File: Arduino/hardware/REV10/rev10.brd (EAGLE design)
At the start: 68.6 x 53.3 mm, 43 parts, among them IC2 ATMEGA168-AU, Q1 32768Hz, Q2 BSS84, U1 TC1185SMD, U2 ARDUINOR3-DIMENSION

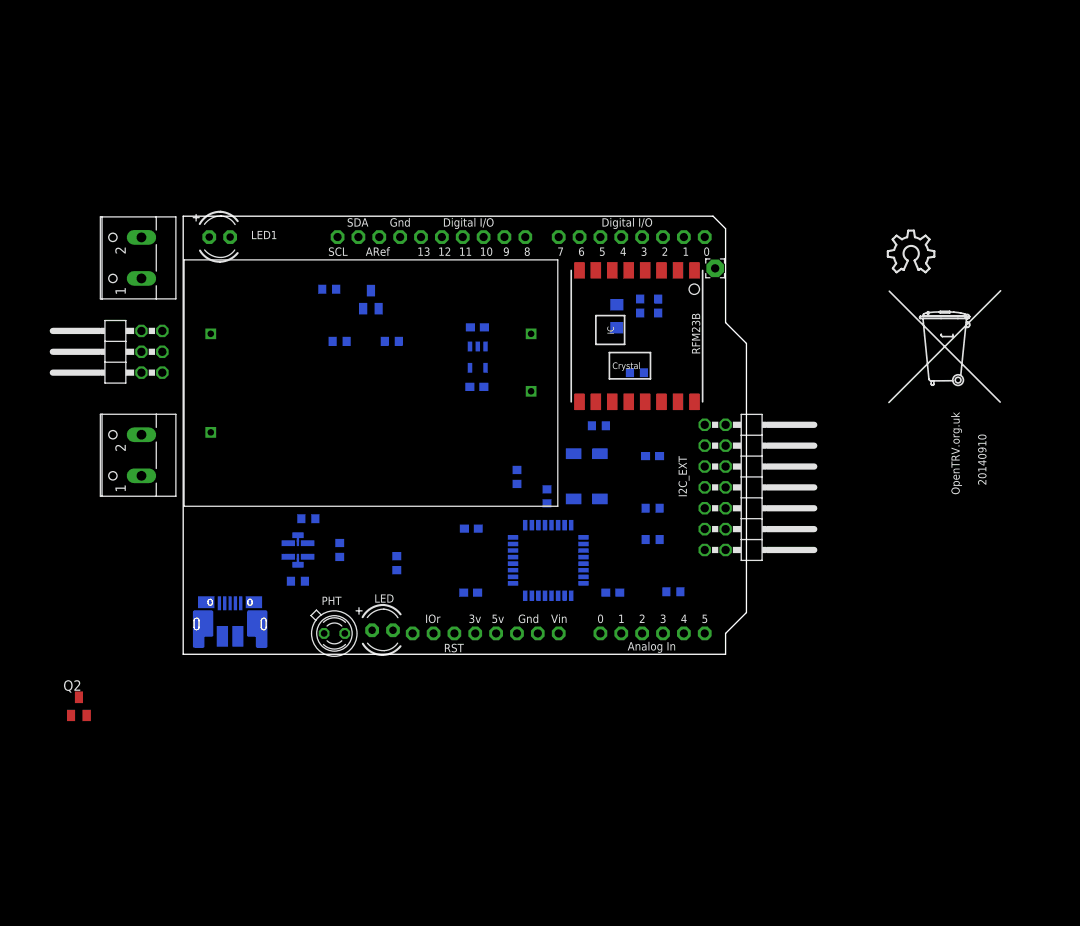
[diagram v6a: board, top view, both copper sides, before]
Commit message: added relay on board
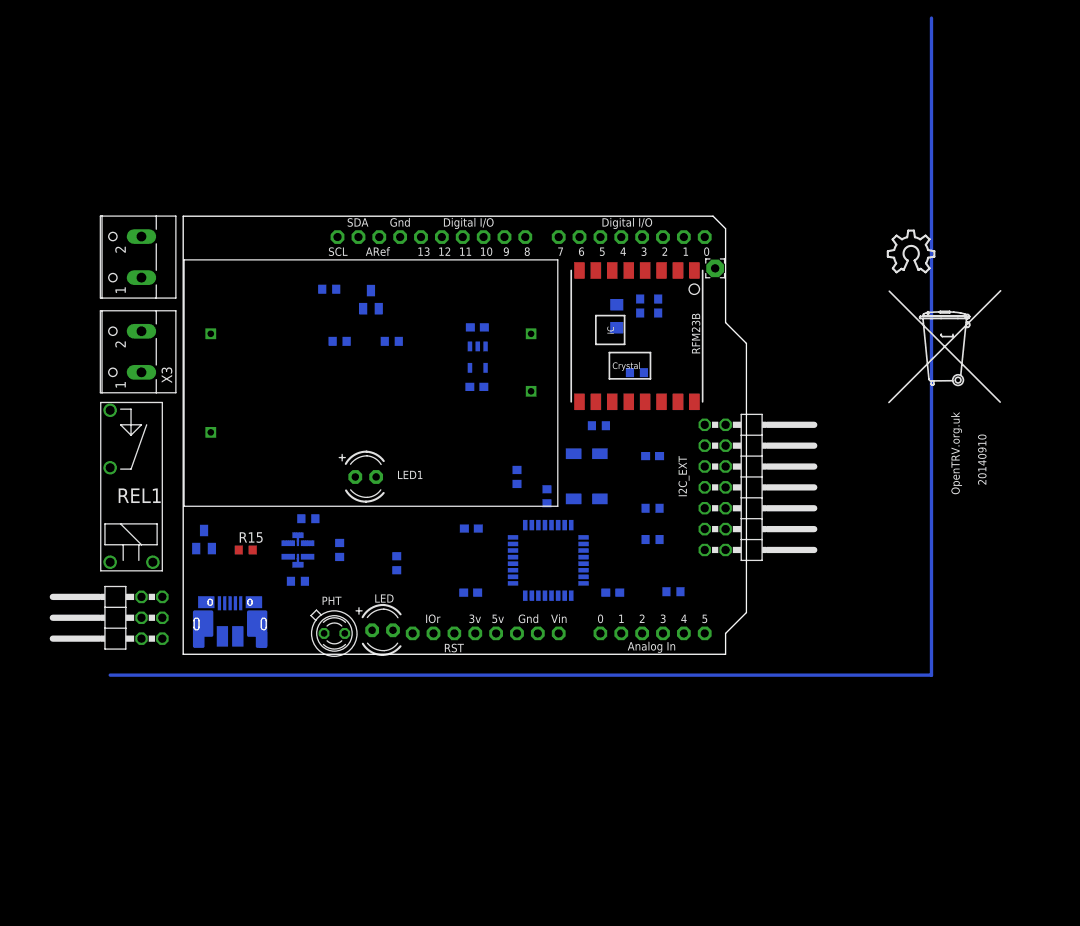
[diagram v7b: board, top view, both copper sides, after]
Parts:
- removed X2: (no value), con-wago-500:W237-102
- added R15: 4.7K, resistor:R0603
- added REL1: (no value), ALDP105:ALDP105
- added X3: (no value), con-wago-500:W237-102
- moved LED1 34.2 mm to (31.1, 21.6)
- moved JP2 32.4 mm to (0.00, 4.45)
- moved Q2 25.4 mm to (11.4, 14.0), flipped to the bottom
- moved X1 24.1 mm to (2.54, 48.4)
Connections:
- new net 5VGSM: Q2.3
- new net N$17: Q2.1, R15.1
- new net N$22: REL1.C, X3.2
- new net N$24: REL1.S, X3.1
- new net PFET: R15.2
- net 5V: now also Q2.2, REL1.S2; no longer X2.2
- net N$14: now also REL1.S1; no longer X2.1
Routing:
- net N$21: track 0.00 -> 180.0 mm

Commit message: before routing update
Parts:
- REL1: device ALDP105:ALDP105 -> OJE-SS-103HM:OJE-SS-103HM
- moved U$1 18.0 mm to (107.4, 33.8)
- moved U$2 12.7 mm to (109.1, 44.9)
- moved ANT1 7.62 mm to (81.3, 47.0)
- moved C2 7.62 mm to (52.3, 32.6)
- moved C7 7.62 mm to (74.3, 42.4)
- moved C9 7.62 mm to (51.6, 15.3)
- moved I2C_EXT 7.62 mm to (86.4, 20.3)
- moved Q1 7.62 mm to (65.6, 21.7)
- moved R9 7.62 mm to (76.2, 7.62)
- moved LED1 7.62 mm to (38.7, 21.6)
- moved Q2 7.62 mm to (19.1, 14.0)
- moved R13 7.62 mm to (35.6, 38.1)
- moved R4 7.62 mm to (31.8, 16.5)
- moved R6 7.62 mm to (30.5, 8.89)
- moved R8 7.62 mm to (35.6, 12.7)
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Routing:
- net N$21: track 180.0 -> 286.3 mm
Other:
- board size 68.6 x 53.3 mm -> 8.8 x 3.7 mm
